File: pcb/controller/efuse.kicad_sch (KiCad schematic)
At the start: 12 parts, among them U5 TPS25942ARVCR

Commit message: retraced target pcb
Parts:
- C12: footprint (none) -> Capacitor_SMD:C_1206_3216Metric
- R14, R17, R18: footprint (none) -> Resistor_SMD:R_1206_3216Metric
- R15: value 6,49k -> 6.49k; footprint (none) -> Resistor_SMD:R_1206_3216Metric
- R16: value 26,7k -> 26.7k; footprint (none) -> Resistor_SMD:R_1206_3216Metric
- R19: value 42,2k -> 42.2k; footprint (none) -> Resistor_SMD:R_1206_3216Metric
- R20: value 8,66k -> 8.66k; footprint (none) -> Resistor_SMD:R_1206_3216Metric
- R21: value 1,5k -> 1.5k; footprint (none) -> Resistor_SMD:R_1206_3216Metric
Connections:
- no-connect marks 0 -> 2
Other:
- moved on the sheet: JP2
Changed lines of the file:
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@@
 		(color 0 0 0 0)
 	)
+	(no_connect
+		(at 116.84 101.6)
+	)
+	(no_connect
+		(at 76.2 101.6)
+	)
 	(wire
 		(pts
@@
 	(wire
 		(pts
-			(xy 130.81 55.88) (xy 130.81 91.44)
-		)
-		(stroke
-			(width 0)
-			(type default)
-		)
-	)
-	(wire
-		(pts
-			(xy 120.65 109.22) (xy 121.92 109.22)
-		)
-		(stroke
-			(width 0)
-			(type default)
-		)
-	)
-	(wire
-		(pts
-			(xy 92.71 55.88) (xy 69.85 55.88)
+			(xy 130.81 67.31) (xy 130.81 91.44)
+		)
+		(stroke
+			(width 0)
+			(type default)
+		)
+	)
+	(wire
+		(pts
+			(xy 120.65 109.22) (xy 123.19 109.22)
+		)
+		(stroke
+			(width 0)
+			(type default)
+		)
+	)
+	(wire
+		(pts
+			(xy 88.9 67.31) (xy 69.85 67.31)
 		)
 		(stroke
@@
 	(wire
 		(pts
-			(xy 100.33 55.88) (xy 130.81 55.88)
+			(xy 96.52 67.31) (xy 130.81 67.31)
 		)
 		(stroke
@@
 	(wire
 		(pts
-			(xy 69.85 55.88) (xy 69.85 78.74)
+			(xy 69.85 67.31) (xy 69.85 78.74)
 		)
 		(stroke
@@
 	(hierarchical_label "Imon"
 		(shape output)
-		(at 121.92 109.22 0)
+		(at 123.19 109.22 0)
 		(effects
 			(font
@@
 			)
 		)
-		(property "Value" "1,5k"
+		(property "Value" "1.5k"
 			(at 85.09 74.93 90)
 			(effects
@@
 			)
 		)
-		(property "Footprint" ""
+		(property "Footprint" "Resistor_SMD:R_1206_3216Metric"
 			(at 85.09 80.518 90)
 			(effects
@@
 			)
 		)
-		(property "Value" "6,49k"
+		(property "Value" "6.49k"
 			(at 55.88 104.1399 0)
 			(effects
@@
 			)
 		)
-		(property "Footprint" ""
+		(property "Footprint" "Resistor_SMD:R_1206_3216Metric"
 			(at 51.562 102.87 90)
 			(effects
@@
 			)
 		)
-		(property "Value" "42,2k"
+		(property "Value" "42.2k"
 			(at 133.35 111.7599 0)
 			(effects
@@
 			)
 		)
-		(property "Footprint" ""
+		(property "Footprint" "Resistor_SMD:R_1206_3216Metric"
 			(at 129.032 110.49 90)
 			(effects
@@
 	(symbol
 		(lib_id "Jumper:SolderJumper_2_Open")
-		(at 96.52 55.88 0)
+		(at 92.71 67.31 0)
 		(unit 1)
 		(exclude_from_sim no)
@@
 		(fields_autoplaced yes)
 		(property "Reference" "JP2"
-			(at 96.52 49.53 0)
+			(at 92.71 60.96 0)
 			(effects
 				(font
@@
 		)
 		(property "Value" "SolderJumper_2_Open"
-			(at 96.52 52.07 0)
+			(at 92.71 63.5 0)
 			(effects
 				(font
@@
 		)
 		(property "Footprint" "Jumper:SolderJumper-2_P1.3mm_Open_Pad1.0x1.5mm"
-			(at 96.52 55.88 0)
+			(at 92.71 67.31 0)
 			(effects
 				(font
@@
 		)
 		(property "Datasheet" "~"
-			(at 96.52 55.88 0)
+			(at 92.71 67.31 0)
 			(effects
 				(font
@@
 		)
 		(property "Description" "Solder Jumper, 2-pole, open"
-			(at 96.52 55.88 0)
+			(at 92.71 67.31 0)
 			(effects
 				(font
@@
 			)
 		)
-		(property "Footprint" ""
+		(property "Footprint" "Resistor_SMD:R_1206_3216Metric"
 			(at 71.882 120.65 90)
 			(effects
@@
 			)
 		)
-		(property "Footprint" ""
+		(property "Footprint" "Resistor_SMD:R_1206_3216Metric"
 			(at 123.952 95.25 90)
 			(effects
@@
 			)
 		)
-		(property "Footprint" ""
+		(property "Footprint" "Capacitor_SMD:C_1206_3216Metric"
 			(at 68.8848 116.84 0)
 			(effects
@@
 			)
 		)
-		(property "Footprint" ""
+		(property "Footprint" "Resistor_SMD:R_1206_3216Metric"
 			(at 51.562 95.25 90)
 			(effects
@@
 			)
 		)
-		(property "Value" "8,66k"
+		(property "Value" "8.66k"
 			(at 123.19 115.5699 0)
 			(effects
@@
 			)
 		)
-		(property "Footprint" ""
+		(property "Footprint" "Resistor_SMD:R_1206_3216Metric"
 			(at 118.872 114.3 90)
 			(effects
@@
 			)
 		)
-		(property "Value" "26,7k"
+		(property "Value" "26.7k"
 			(at 55.88 111.7599 0)
 			(effects
@@
 			)
 		)
-		(property "Footprint" ""
+		(property "Footprint" "Resistor_SMD:R_1206_3216Metric"
 			(at 51.562 110.49 90)
 			(effects

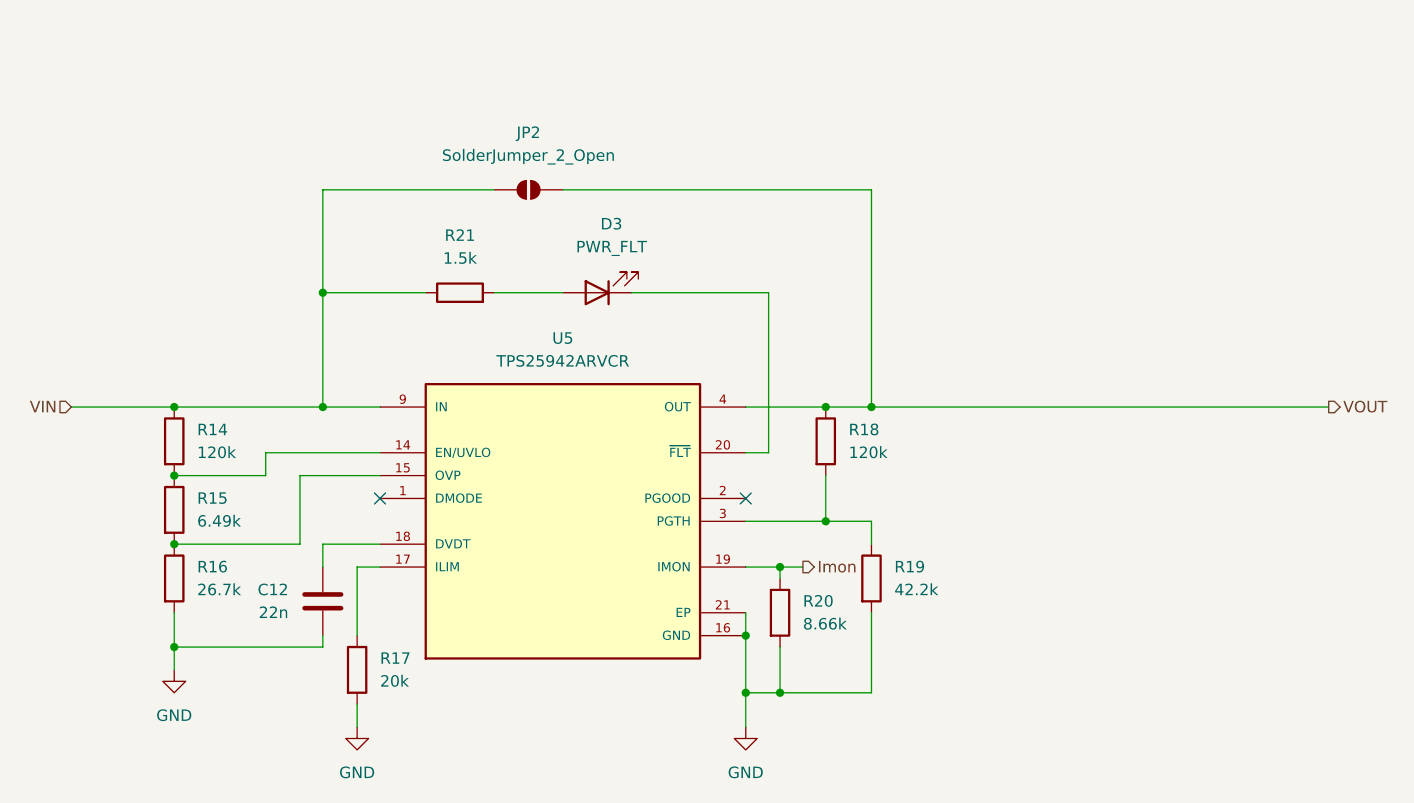
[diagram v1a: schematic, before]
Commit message: added lcsc numbers to all components and added ESD protection
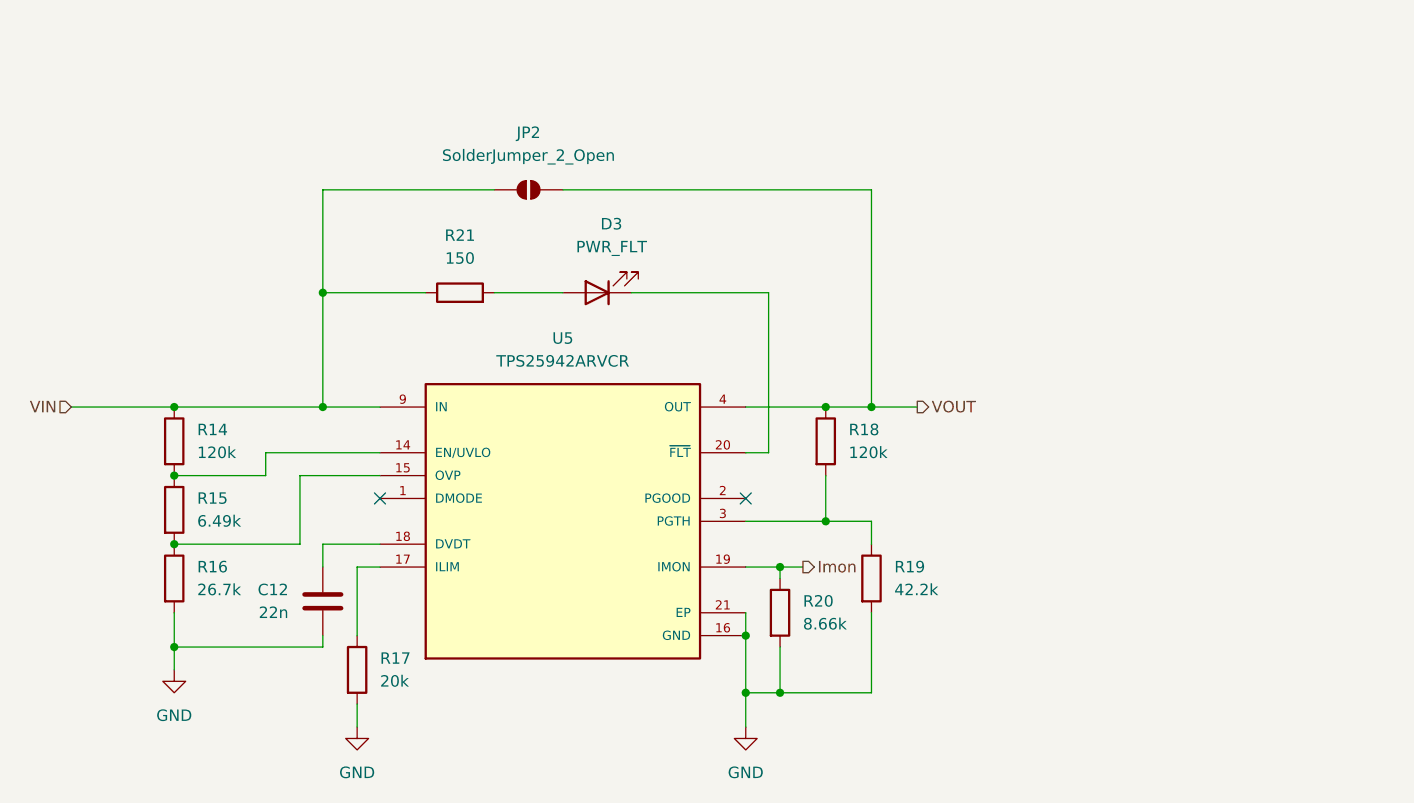
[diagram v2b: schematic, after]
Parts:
- C12: footprint Capacitor_SMD:C_1206_3216Metric -> Capacitor_SMD:C_0805_2012Metric; LCSC (none) -> C1729
- D3: footprint (none) -> LED_SMD:LED_0603_1608Metric; LCSC (none) -> C51933292
- R14, R18: footprint Resistor_SMD:R_1206_3216Metric -> Resistor_SMD:R_0805_2012Metric; LCSC (none) -> C17436
- R15: footprint Resistor_SMD:R_1206_3216Metric -> Resistor_SMD:R_0805_2012Metric; LCSC (none) -> C2933484
- R16: footprint Resistor_SMD:R_1206_3216Metric -> Resistor_SMD:R_0805_2012Metric; LCSC (none) -> C2999467
- R17: footprint Resistor_SMD:R_1206_3216Metric -> Resistor_SMD:R_0805_2012Metric; LCSC (none) -> C2907240
- R19: footprint Resistor_SMD:R_1206_3216Metric -> Resistor_SMD:R_0805_2012Metric; LCSC (none) -> C5119971
- R20: footprint Resistor_SMD:R_1206_3216Metric -> Resistor_SMD:R_0805_2012Metric; LCSC (none) -> C2933506
- R21: value 1.5k -> 150; footprint Resistor_SMD:R_1206_3216Metric -> Resistor_SMD:R_0603_1608Metric; LCSC (none) -> C2907103
- U5: footprint TPS25942ARVCR:IC_TPS25942ARVCR -> external_footprints.petty:IC_TPS25942ARVCR
